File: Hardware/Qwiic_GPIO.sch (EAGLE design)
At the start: 35 parts, among them J2 SMD, J3 PTH, J4 SMD, J7 455-1750-1-ND, U3 TCA9534

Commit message: Updating address jumper note
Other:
- note added: "0 0 0 0x20"
- note added: "1 1 1 0x27 (default)"
- note removed: "0 0 0 0x20 (default)"
- note removed: "1 1 1 0x27"
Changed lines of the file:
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@@
 <text x="5.08" y="68.58" size="2.54" layer="94" font="vector">Address Selection Jumpers</text>
 <text x="66.04" y="55.88" size="1.778" layer="97" font="vector">A2   A1  A0  Address</text>
-<text x="66.04" y="50.8" size="2.032" layer="97" font="vector">0   0   0   0x20 (default)</text>
+<text x="66.04" y="50.8" size="2.032" layer="97" font="vector">0   0   0   0x20</text>
 <text x="66.04" y="45.72" size="2.032" layer="97" font="vector">0   0   1   0x21</text>
 <text x="66.04" y="40.64" size="2.032" layer="97" font="vector">0   1   0   0x22</text>
@@
 <text x="66.04" y="25.4" size="2.032" layer="97" font="vector">1   0   1   0x25</text>
 <text x="66.04" y="20.32" size="2.032" layer="97" font="vector">1   1   0   0x26</text>
-<text x="66.04" y="15.24" size="2.032" layer="96" font="vector">1   1   1   0x27</text>
+<text x="66.04" y="15.24" size="2.032" layer="96" font="vector">1   1   1   0x27 (default)</text>
 <wire x1="63.5" y1="58.42" x2="63.5" y2="54.61" width="0.2032" layer="97"/>
 <wire x1="63.5" y1="54.61" x2="63.5" y2="49.53" width="0.2032" layer="97"/>

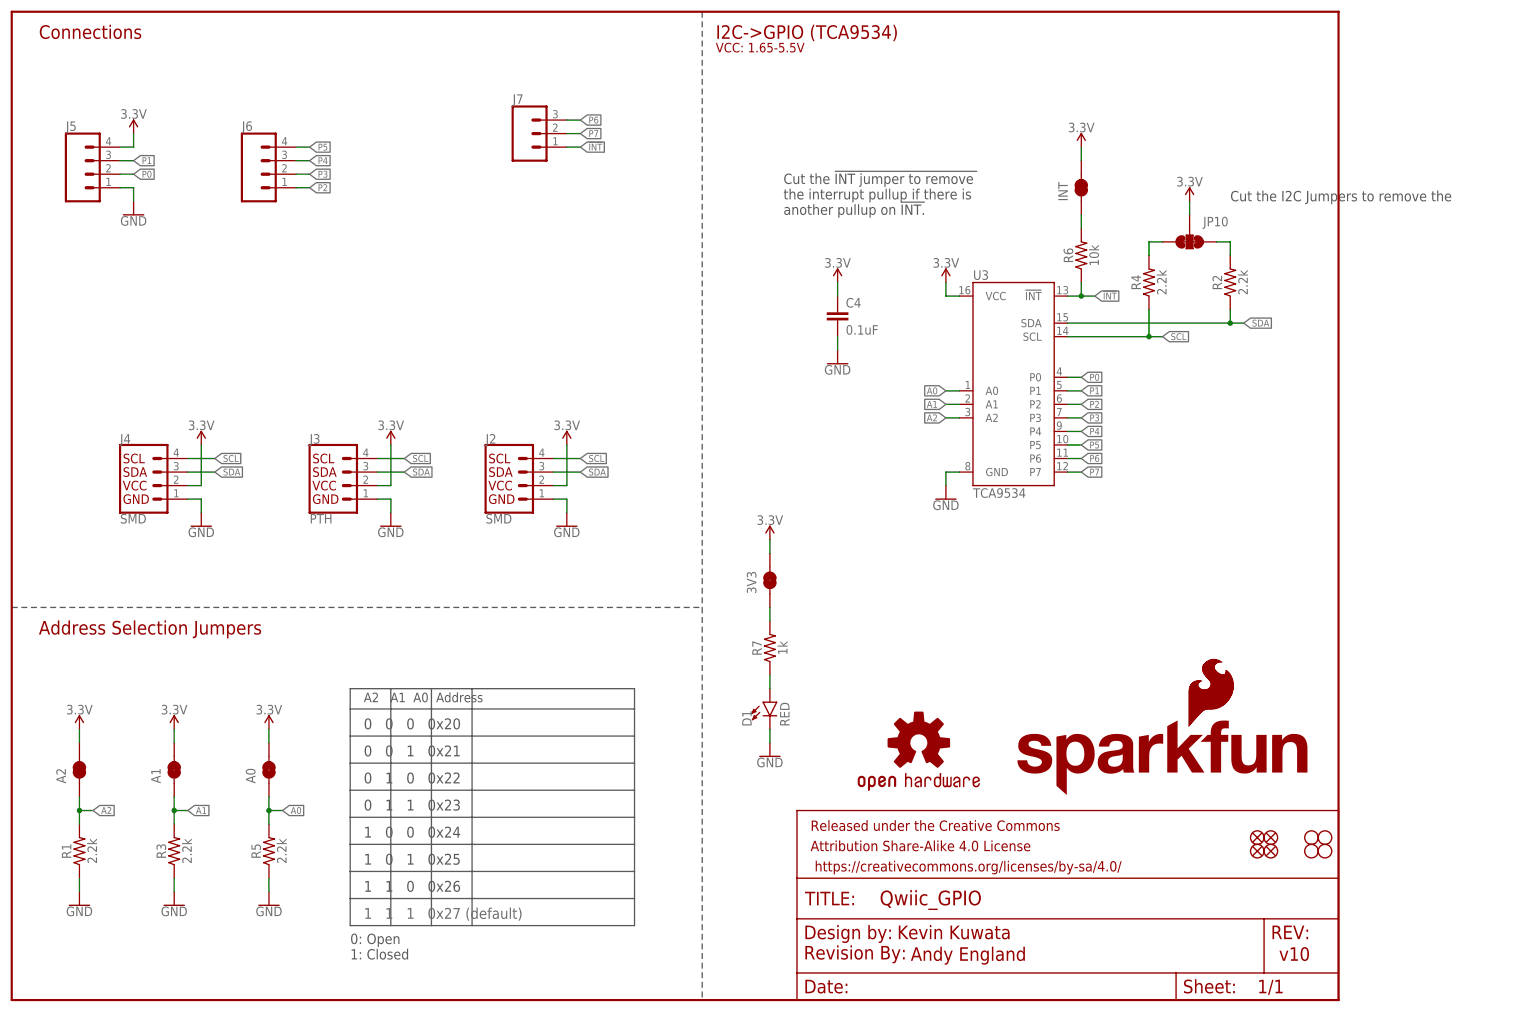
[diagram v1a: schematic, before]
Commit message: adding rest of GPIO pins
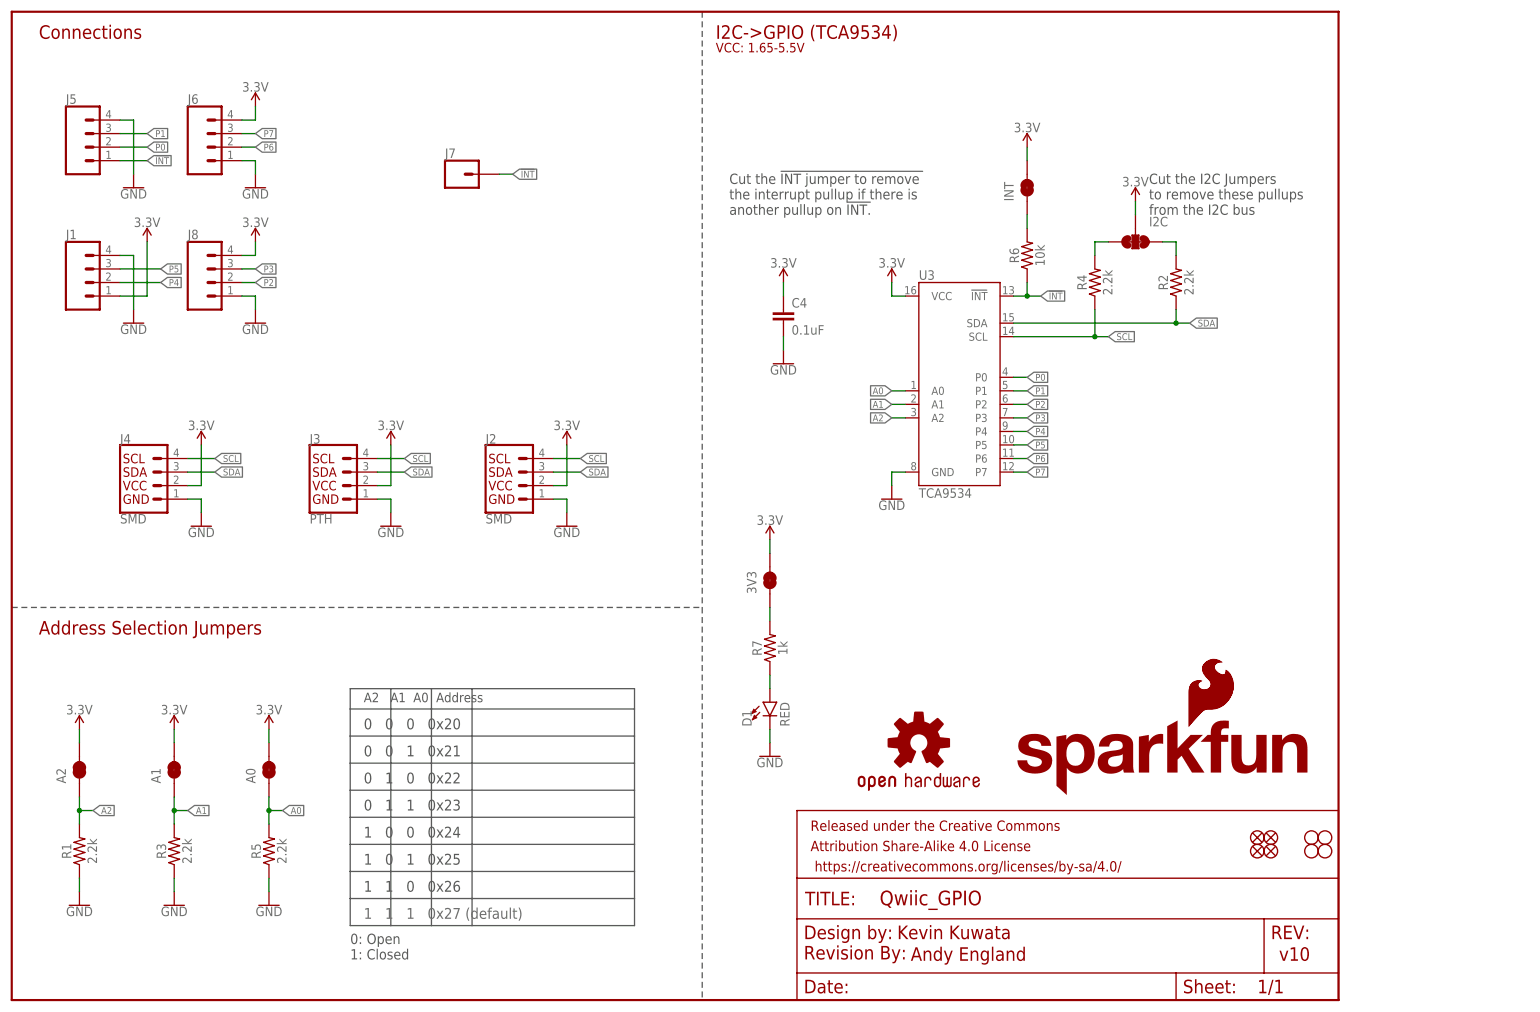
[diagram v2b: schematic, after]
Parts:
- removed JP10: JUMPER-SMT_3_2-NC_TRACE_SILK, SparkFun-Jumpers:JUMPER-SMT_3_2-NC_TRACE_SILK
- added I2C: JUMPER-SMT_3_2-NC_TRACE_SILK, SparkFun-Jumpers:JUMPER-SMT_3_2-NC_TRACE_SILK
- added J1, J8: (no value), SparkFun-Connectors:CONN_04LATCH
- J7: value 455-1750-1-ND -> (none); device SparkFun-Connectors:CONN_031X03_NO_SILK -> SparkFun-Connectors:CONN_01PTH_NO_SILK_YES_STOP
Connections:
- net !INT: now also J5.1
- net 3.3V: now also I2C.2, J1.1, J6.4, J8.4; no longer J5.4, JP10.2
- net GND: now also J1.4, J5.4, J6.1, J8.1; no longer J5.1
- net P2: now also J8.2; no longer J6.1
- net P3: now also J8.3; no longer J6.2
- net P4: now also J1.2; no longer J6.3
- net P5: now also J1.3; no longer J6.4
- net P6: now also J6.2; no longer J7.3
- net P7: now also J6.3; no longer J7.2
- net SCL_PU1: now also I2C.1; no longer JP10.1
- net SDA_PU1: now also I2C.3; no longer JP10.3
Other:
- note added: "Cut the I2C Jumpers to remove these pullups from the I2C bus"
- note removed: "Cut the I2C Jumpers to remove the"
- moved on the sheet: C4, INT, J5, J6, R2, R4, R6, U3

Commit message: post checklist changes
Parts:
- removed J3: PTH, SparkX:I2C_STANDARD_NO_SILK
- added J9: (no value), SparkFun-Connectors:CONN_041X04_NO_SILK
- J2, J4: value SMD -> QWIIC; device SparkX:I2C_STANDARDJS-1MM -> SparkFun-Connectors:QWIIC_CONNECTORJS-1MM
- renumbered 3V3 to PWR, A0 to ADR0, A1 to ADR1, A2 to ADR2
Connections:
- net A0 renamed ADR0
- net A1 renamed ADR1
- net A2 renamed ADR2
- net 3.3V: now also J2.2, J4.2, J9.2; no longer J2.VCC, J3.VCC, J4.VCC
- net GND: now also J2.1, J4.1, J9.1; no longer J2.GND, J3.GND, J4.GND
- net SCL: now also J2.4, J4.4, J9.4; no longer J2.SCL, J3.SCL, J4.SCL
- net SDA: now also J2.3, J4.3, J9.3; no longer J2.SDA, J3.SDA, J4.SDA
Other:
- note added: "ADR2 ADR1 ADR0 Address"
- note added: "Cut the PWR Jumper to disable the PWR LED"
- note removed: "A2 A1 A0 Address"
- moved on the sheet: C4, I2C, INT, R2, R4, R6, U3
